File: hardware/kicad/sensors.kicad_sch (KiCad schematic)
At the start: 8 parts, among them U4 LSM6DSOTR, U5 MAX17048G+

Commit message: wip: revision 2
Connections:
- net +3.3V renamed +3V3
- net MAX17048_INT renamed FG_INT
- net MAX17048_SCL renamed FG_SCL
- net MAX17048_SDA renamed FG_SDA
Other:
- note added: "Sheets Connection"
- moved on the sheet: C10, C11, C12, C9, R10, U5

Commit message: wip: revision 2
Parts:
- added J6: Qwiic, bwlr1e:JST_SH_SM04B-SRSS-TB_1x04-1MP_P1.00mm_Horizontal, symbol Connector_Generic:Conn_01x04
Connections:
- net IMU_SCL is gone; now on net SCL: U4.13 (SCL)
- net IMU_SDA is gone; now on net SDA: U4.14 (SDA)
- net +3V3: now also J6.2 (Pin_2)
- net GND: now also J6.1 (Pin_1)
- net FG_SCL renamed SCL
- net SCL: now also J6.4 (Pin_4)
- net FG_SDA renamed SDA
- net SDA: now also J6.3 (Pin_3)
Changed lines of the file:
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@@
+    (stroke (width 0) (type default))
+  )
+  (wire (pts (xy 159.385 52.705) (xy 159.385 55.245))
     (stroke (width 0) (type default))
   )
@@
     (stroke (width 0) (type default))
   )
+  (wire (pts (xy 166.37 57.785) (xy 166.37 59.055))
+    (stroke (width 0) (type default))
+  )
   (wire (pts (xy 191.77 105.41) (xy 191.77 104.14))
     (stroke (width 0) (type default))
@@
     (stroke (width 0) (type default))
   )
+  (wire (pts (xy 159.385 55.245) (xy 175.26 55.245))
+    (stroke (width 0) (type default))
+  )
   (wire (pts (xy 117.602 57.15) (xy 117.602 54.61))
     (stroke (width 0) (type default))
@@
   )
   (wire (pts (xy 72.898 102.362) (xy 84.328 102.362))
+    (stroke (width 0) (type default))
+  )
+  (wire (pts (xy 166.37 57.785) (xy 175.26 57.785))
     (stroke (width 0) (type default))
   )
@@
     (effects (font (size 1.27 1.27)) (justify left bottom))
   )
-  (hierarchical_label "IMU_SCL" (shape input) (at 82.55 99.06 180) (fields_autoplaced)
+  (hierarchical_label "SCL" (shape input) (at 82.55 99.06 180) (fields_autoplaced)
     (effects (font (size 1.27 1.27)) (justify right))
   )
-  (hierarchical_label "FG_SDA" (shape bidirectional) (at 153.67 99.06 180) (fields_autoplaced)
+  (hierarchical_label "SDA" (shape bidirectional) (at 175.26 52.705 180) (fields_autoplaced)
+    (effects (font (size 1.27 1.27)) (justify right))
+  )
+  (hierarchical_label "SCL" (shape input) (at 175.26 50.165 180) (fields_autoplaced)
     (effects (font (size 1.27 1.27)) (justify right))
   )
@@
     (effects (font (size 1.27 1.27)) (justify right))
   )
-  (hierarchical_label "IMU_SDA" (shape bidirectional) (at 82.55 96.774 180) (fields_autoplaced)
+  (hierarchical_label "SDA" (shape bidirectional) (at 82.55 96.774 180) (fields_autoplaced)
     (effects (font (size 1.27 1.27)) (justify right))
   )
-  (hierarchical_label "FG_SCL" (shape input) (at 153.67 96.52 180) (fields_autoplaced)
+  (hierarchical_label "SCL" (shape input) (at 153.67 96.52 180) (fields_autoplaced)
     (effects (font (size 1.27 1.27)) (justify right))
   )
@@
   )
   (hierarchical_label "+BATT" (shape input) (at 129.54 136.652 180) (fields_autoplaced)
+    (effects (font (size 1.27 1.27)) (justify right))
+  )
+  (hierarchical_label "SDA" (shape bidirectional) (at 153.67 99.06 180) (fields_autoplaced)
     (effects (font (size 1.27 1.27)) (justify right))
   )
@@
     )
   )
+  (symbol (lib_id "Connector_Generic:Conn_01x04") (at 180.34 55.245 0) (mirror x) (unit 1)
+    (in_bom yes) (on_board yes) (dnp no)
+    (property "Reference" "J6" (at 183.515 55.245 0)
+      (effects (font (size 1.27 1.27)) (justify left))
+    )
+    (property "Value" "Qwiic" (at 183.515 52.705 0)
+      (effects (font (size 1.27 1.27)) (justify left))
+    )
+    (property "Footprint" "bwlr1e:JST_SH_SM04B-SRSS-TB_1x04-1MP_P1.00mm_Horizontal" (at 180.34 55.245 0)
+      (effects (font (size 1.27 1.27)) hide)
+    )
+    (property "Datasheet" "https://datasheet.lcsc.com/lcsc/2304140030_JST-Sales-America-SM04B-SRSS-TB-LF-SN_C160404.pdf" (at 180.34 55.245 0)
+      (effects (font (size 1.27 1.27)) hide)
+    )
+    (property "Manufacturer" "JST Sales America" (at 180.34 55.245 0)
+      (effects (font (size 1.27 1.27)) hide)
+    )
+    (property "Part Number" "SM04B-SRSS-TB" (at 180.34 55.245 0)
+      (effects (font (size 1.27 1.27)) hide)
+    )
+    (property "Part Description" "" (at 180.34 55.245 0)
+      (effects (font (size 1.27 1.27)) hide)
+    )
+    (property "Manufacturer Part Number" "" (at 180.34 55.245 0)
+      (effects (font (size 1.27 1.27)) hide)
+    )
+    (property "Distributor" "" (at 180.34 55.245 0)
+      (effects (font (size 1.27 1.27)) hide)
+    )
+    (property "Distributor Part Number" "" (at 180.34 55.245 0)
+      (effects (font (size 1.27 1.27)) hide)
+    )
+    (property "Distributor Link" "" (at 180.34 55.245 0)
+      (effects (font (size 1.27 1.27)) hide)
+    )
+    (pin "1")
+    (pin "2")
+    (pin "3")
+    (pin "4")
+    (instances
+      (project "bwlc1a"
+        (path "/388039b1-99cc-430f-bd4a-010573fde798/f0ceb3a9-6c16-45f6-8aec-9ac0bb10996d"
+          (reference "J6") (unit 1)
+        )
+      )
+      (project "bwlr1e"
+        (path "/630c8da6-5464-4eef-824d-89618087f4b4"
+          (reference "J1") (unit 1)
+        )
+      )
+    )
+  )
   (symbol (lib_id "Device:C_Small") (at 107.442 59.69 0) (unit 1)
     (in_bom yes) (on_board yes) (dnp no) (fields_autoplaced)
@@
         )
       )
+    )
+  )
+  (symbol (lib_id "power:GND") (at 166.37 59.055 0) (unit 1)
+    (in_bom yes) (on_board yes) (dnp no) (fields_autoplaced)
+    (property "Reference" "#PWR0115" (at 166.37 65.405 0)
+      (effects (font (size 1.27 1.27)) hide)
+    )
+    (property "Value" "GND" (at 166.37 64.135 0)
+      (effects (font (size 1.27 1.27)))
+    )
+    (property "Footprint" "" (at 166.37 59.055 0)
+      (effects (font (size 1.27 1.27)) hide)
+    )
+    (property "Datasheet" "" (at 166.37 59.055 0)
+      (effects (font (size 1.27 1.27)) hide)
+    )
+    (pin "1")
+    (instances
+      (project "bwlc1a"
+        (path "/388039b1-99cc-430f-bd4a-010573fde798/f0ceb3a9-6c16-45f6-8aec-9ac0bb10996d"
+          (reference "#PWR0115") (unit 1)
+        )
+      )
+      (project "bwlr1e"
+        (path "/630c8da6-5464-4eef-824d-89618087f4b4"
+          (reference "#PWR05") (unit 1)
+        )
+      )
+    )
+  )
+  (symbol (lib_id "power:+3V3") (at 159.385 52.705 0) (mirror y) (unit 1)
+    (in_bom yes) (on_board yes) (dnp no)
+    (property "Reference" "#PWR0113" (at 159.385 56.515 0)
+      (effects (font (size 1.27 1.27)) hide)
+    )
+    (property "Value" "+3V3" (at 153.035 51.435 0)
+      (effects (font (size 1.27 1.27)) (justify right))
+    )
+    (property "Footprint" "" (at 159.385 52.705 0)
+      (effects (font (size 1.27 1.27)) hide)
+    )
+    (property "Datasheet" "" (at 159.385 52.705 0)
+      (effects (font (size 1.27 1.27)) hide)
+    )
+    (pin "1")
+    (instances
+      (project "bwlc1a"
+        (path "/388039b1-99cc-430f-bd4a-010573fde798/f0ceb3a9-6c16-45f6-8aec-9ac0bb10996d"
+          (reference "#PWR0113") (unit 1)
+        )
+      )
+      (project "bwlr1e"
+        (path "/630c8da6-5464-4eef-824d-89618087f4b4"
+          (reference "#PWR07") (unit 1)
+        )
+      )

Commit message: wip: revision 2
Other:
- note added: "Qwiic Port"
- note added: "Sleep mode: 0.5µA Hibernate mode: 4uA Active mode: 23uA"
- note removed: "- Sleep mode: 0.5µA - Hibernate mode: 4uA - Active mode: 23uA ( auto switch to hibernate )"
- moved on the sheet: C10, C11, C12, C8, C9, J6, R10, U4, U5

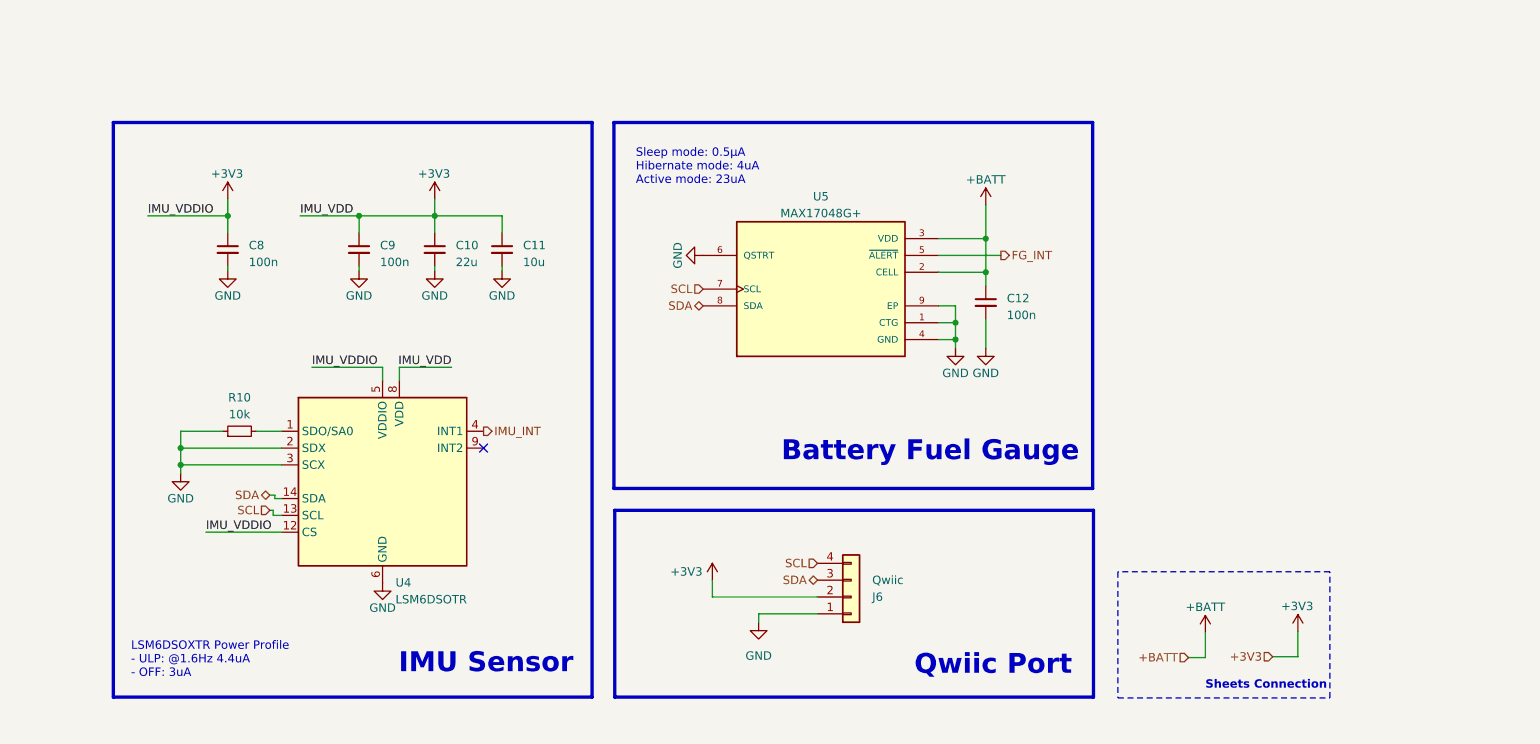
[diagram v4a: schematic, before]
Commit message: clean-up and update antenna
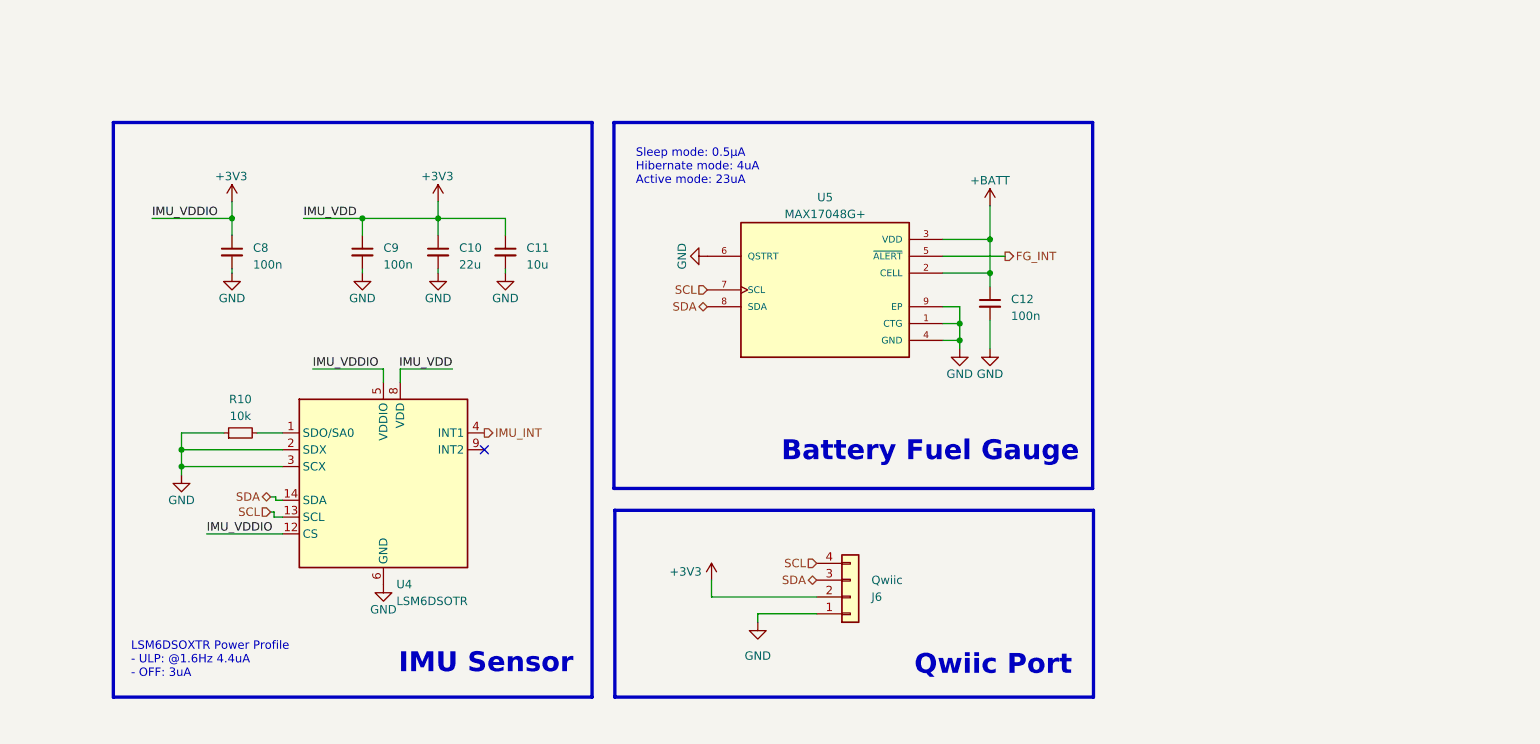
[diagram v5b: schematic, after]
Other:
- note removed: "Sheets Connection"
- moved on the sheet: C10, C11, C12, C8, C9, U5

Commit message: Early PCB Layouting
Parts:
- J6: footprint bwlr1e:JST_SH_SM04B-SRSS-TB_1x04-1MP_P1.00mm_Horizontal -> Connector_JST:JST_SH_SM04B-SRSS-TB_1x04-1MP_P1.00mm_Horizontal
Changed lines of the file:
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@@
       (effects (font (size 1.27 1.27)) (justify left))
     )
-    (property "Footprint" "bwlr1e:JST_SH_SM04B-SRSS-TB_1x04-1MP_P1.00mm_Horizontal" (at 179.07 122.555 0)
+    (property "Footprint" "Connector_JST:JST_SH_SM04B-SRSS-TB_1x04-1MP_P1.00mm_Horizontal" (at 179.07 122.555 0)
       (effects (font (size 1.27 1.27)) hide)
     )

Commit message: PCB Layout Update
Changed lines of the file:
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@@
     (stroke (width 0) (type default))
   )
-  (wire (pts (xy 165.1 125.095) (xy 165.1 126.365))
+  (wire (pts (xy 158.115 125.095) (xy 158.115 127))
     (stroke (width 0) (type default))
   )
@@
     (stroke (width 0) (type default))
   )
-  (wire (pts (xy 165.1 125.095) (xy 173.99 125.095))
+  (wire (pts (xy 158.115 125.095) (xy 173.99 125.095))
     (stroke (width 0) (type default))
   )
@@
     )
   )
-  (symbol (lib_id "power:GND") (at 165.1 126.365 0) (unit 1)
+  (symbol (lib_id "power:GND") (at 158.115 127 0) (unit 1)
     (in_bom yes) (on_board yes) (dnp no) (fields_autoplaced)
-    (property "Reference" "#PWR0115" (at 165.1 132.715 0)
-      (effects (font (size 1.27 1.27)) hide)
-    )
-    (property "Value" "GND" (at 165.1 131.445 0)
-      (effects (font (size 1.27 1.27)))
-    )
-    (property "Footprint" "" (at 165.1 126.365 0)
-      (effects (font (size 1.27 1.27)) hide)
-    )
-    (property "Datasheet" "" (at 165.1 126.365 0)
-      (effects (font (size 1.27 1.27)) hide)
-    )
+    (property "Reference" "#PWR0115" (at 158.115 133.35 0)
+      (effects (font (size 1.27 1.27)) hide)
+    )
+    (property "Value" "GND" (at 158.115 132.08 0)
+      (effects (font (size 1.27 1.27)))
+    )
+    (property "Footprint" "" (at 158.115 127 0)
+      (effects (font (size 1.27 1.27)) hide)
+    )
+    (property "Datasheet" "" (at 158.115 127 0)
+      (effects (font (size 1.27 1.27)) hide)
+    )

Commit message: PCB Layout Update
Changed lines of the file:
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@@
-    (stroke (width 0) (type default))
-  )
-  (wire (pts (xy 92.075 110.49) (xy 93.345 110.49))
     (stroke (width 0) (type default))
   )
@@
     (stroke (width 0) (type default))
   )
-  (wire (pts (xy 91.567 107.442) (xy 92.329 107.442))
+  (wire (pts (xy 90.17 106.045) (xy 90.17 107.95))
     (stroke (width 0) (type default))
   )
@@
     (stroke (width 0) (type default))
   )
+  (wire (pts (xy 88.265 109.22) (xy 88.265 110.49))
+    (stroke (width 0) (type default))
+  )
   (wire (pts (xy 89.535 97.79) (xy 93.345 97.79))
     (stroke (width 0) (type default))
@@
     (stroke (width 0) (type default))
   )
-  (wire (pts (xy 92.075 109.728) (xy 92.075 110.49))
-    (stroke (width 0) (type default))
-  )
   (wire (pts (xy 158.115 120.015) (xy 158.115 122.555))
     (stroke (width 0) (type default))
@@
     (stroke (width 0) (type default))
   )
+  (wire (pts (xy 88.265 110.49) (xy 93.345 110.49))
+    (stroke (width 0) (type default))
+  )
   (wire (pts (xy 97.917 88.138) (xy 108.585 88.138))
     (stroke (width 0) (type default))
@@
     (stroke (width 0) (type default))
   )
-  (wire (pts (xy 91.567 109.728) (xy 92.075 109.728))
+  (wire (pts (xy 86.995 109.22) (xy 88.265 109.22))
     (stroke (width 0) (type default))
   )
@@
     (stroke (width 0) (type default))
   )
-  (wire (pts (xy 92.329 107.95) (xy 93.345 107.95))
+  (wire (pts (xy 86.995 106.045) (xy 90.17 106.045))
     (stroke (width 0) (type default))
   )
@@
     (stroke (width 0) (type default))
   )
-  (wire (pts (xy 92.329 107.442) (xy 92.329 107.95))
-    (stroke (width 0) (type default))
-  )
   (wire (pts (xy 193.04 83.82) (xy 195.58 83.82))
     (stroke (width 0) (type default))
@@
   )
   (wire (pts (xy 127 67.945) (xy 127 65.405))
+    (stroke (width 0) (type default))
+  )
+  (wire (pts (xy 90.17 107.95) (xy 93.345 107.95))
     (stroke (width 0) (type default))
   )
@@
     (effects (font (size 1.27 1.27)) (justify left bottom))
   )
-  (hierarchical_label "SCL" (shape input) (at 91.567 109.728 180) (fields_autoplaced)
+  (hierarchical_label "SCL" (shape input) (at 86.995 109.22 180) (fields_autoplaced)
     (effects (font (size 1.27 1.27)) (justify right))
   )
@@
     (effects (font (size 1.27 1.27)) (justify left))
   )
-  (hierarchical_label "SDA" (shape bidirectional) (at 91.567 107.442 180) (fields_autoplaced)
-    (effects (font (size 1.27 1.27)) (justify right))
-  )
+  (hierarchical_label "SDA" (shape bidirectional) (at 86.995 106.045 180) (fields_autoplaced)
+    (effects (font (size 1.27 1.27)) (justify right))
+  )
